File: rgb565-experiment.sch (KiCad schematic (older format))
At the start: 34 parts, among them J1 ST_SHIFTER_SOCKET, J2 Conn_01x02, SW1 SW_SPDT, U1 74HC00, U2 ST_SHIFTER, U3 ST_SHIFTER, U4 74HC245, U5 74LS257, U6 74HC245

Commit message: almost done routing
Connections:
- net at U1.3: now also U1.13; no longer U1.12
- net at U1.6: now also U1.12; no longer U1.13
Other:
- moved on the sheet: U1A, U1B
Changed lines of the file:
@@
 L 74xx:74HC00 U1
 U 1 1 61BD41CE
+P 9600 2150
+F 0 "U1" H 9600 2200 50  0000 C CNN
+F 1 "74HC00" H 9600 2100 50  0000 C CNN
+F 2 "Package_DIP:DIP-14_W7.62mm_Socket" H 9600 2150 50  0001 C CNN
+F 3 "http://www.ti.com/lit/gpn/sn74hc00" H 9600 2150 50  0001 C CNN
+	1    9600 2150
+	1    0    0    -1
+$EndComp
+$Comp
+L 74xx:74HC00 U1
+U 2 1 61BDB6F9
 P 9600 1700
 F 0 "U1" H 9600 1750 50  0000 C CNN
@@
 F 2 "Package_DIP:DIP-14_W7.62mm_Socket" H 9600 1700 50  0001 C CNN
 F 3 "http://www.ti.com/lit/gpn/sn74hc00" H 9600 1700 50  0001 C CNN
-	1    9600 1700
-	1    0    0    -1
-$EndComp
-$Comp
-L 74xx:74HC00 U1
-U 2 1 61BDB6F9
-P 9600 2150
-F 0 "U1" H 9600 2200 50  0000 C CNN
-F 1 "74HC00" H 9600 2100 50  0000 C CNN
-F 2 "Package_DIP:DIP-14_W7.62mm_Socket" H 9600 2150 50  0001 C CNN
-F 3 "http://www.ti.com/lit/gpn/sn74hc00" H 9600 2150 50  0001 C CNN
-	2    9600 2150
+	2    9600 1700
 	1    0    0    -1
 $EndComp
@@
 	1    0    0    -1
 $EndComp
+Text Label 9000 2050 0    50   ~ 0
+cs
+Wire Wire Line
+	9000 2050 9150 2050
 Text Label 9000 1600 0    50   ~ 0
-cs
-Wire Wire Line
-	9000 1600 9150 1600
-Text Label 9000 2050 0    50   ~ 0
 rxw
 Wire Wire Line
-	9300 2050 9150 2050
+	9300 1600 9150 1600
 Wire Wire Line
 	10900 1800 11500 1800
@@
 	11000 9500 11300 9500
 Wire Wire Line
+	9300 2250 9150 2250
+Wire Wire Line
+	9150 2250 9150 2050
+Connection ~ 9150 2050
+Wire Wire Line
+	9150 2050 9300 2050
+Wire Wire Line
 	9300 1800 9150 1800
 Wire Wire Line
@@
 Connection ~ 9150 1600
 Wire Wire Line
-	9150 1600 9300 1600
-Wire Wire Line
-	9300 2250 9150 2250
-Wire Wire Line
-	9150 2250 9150 2050
-Connection ~ 9150 2050
-Wire Wire Line
-	9150 2050 9000 2050
+	9150 1600 9000 1600
 Wire Wire Line
 	9900 2150 10100 2150

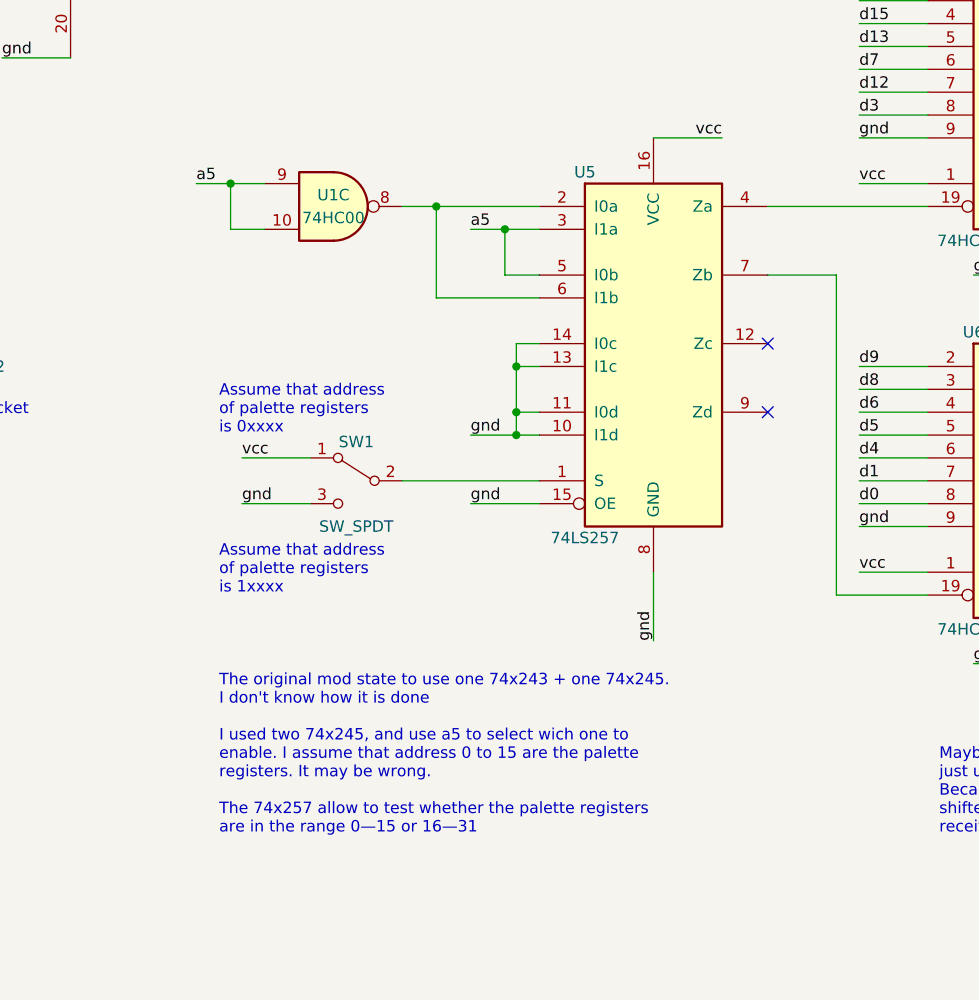
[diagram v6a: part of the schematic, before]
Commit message: Release Candidate 1 : modifications following experiments with the experimental version
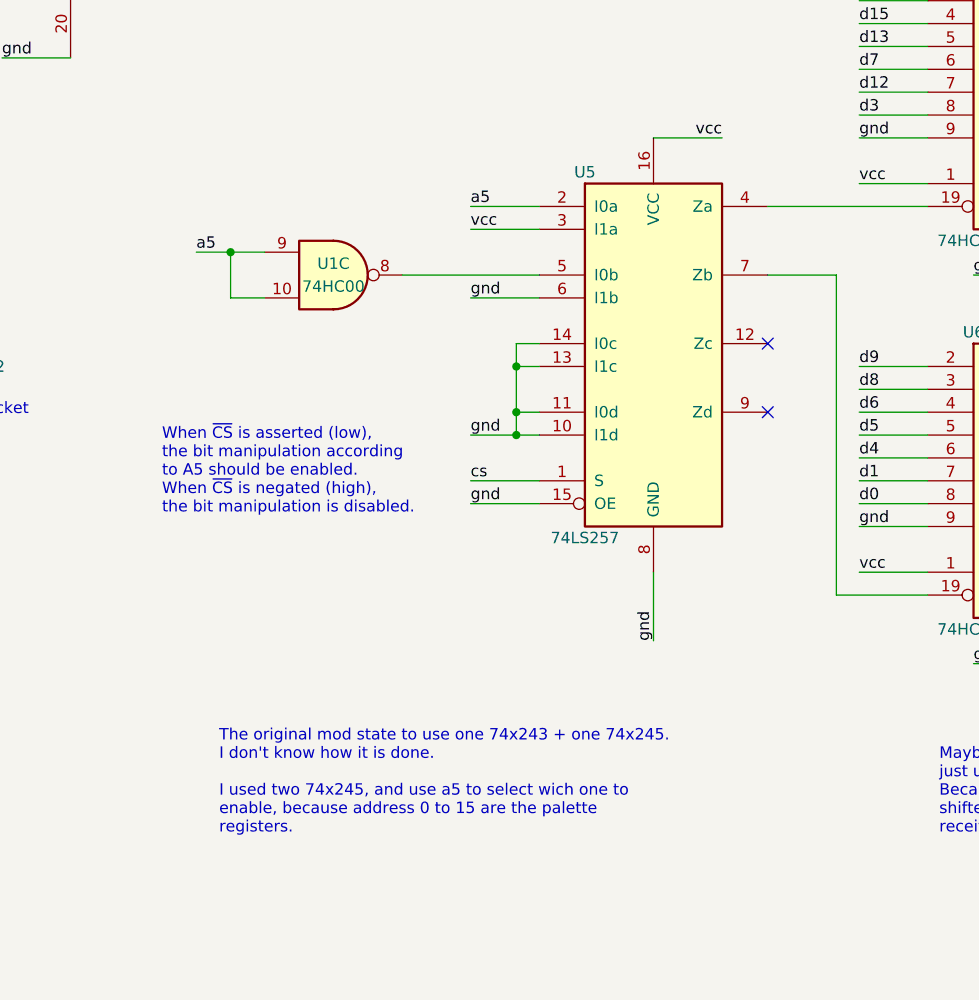
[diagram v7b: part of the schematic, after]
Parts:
- removed SW1: SW_SPDT, Connector_PinHeader_2.54mm:PinHeader_1x03_P2.54mm_Vertical, symbol Switch:SW_SPDT
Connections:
- net +5V: now also U5.3 (I1a)
- net GND: now also U5.6 (I1b)
- net a5: now also U5.2 (I0a); no longer U5.3 (I1a), U5.5 (I0b)
- net cs: now also U5.1 (S)
- new net: U1.8, U5.5 (I0b)
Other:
- note added: "The original mod state to use one 74x243 + one 74x245.\nI don't know how it is done.\n\nI used two 74x245, and use a5 to select wich one to \nenable, because address 0 to 15 are the palette\nregisters."
- note added: "When ~CS~ is asserted (low),\nthe bit manipulation according\nto A5 should be enabled.\nWhen ~CS~ is negated (high),\nthe bit manipulation is disabled."
- note removed: "Assume that address\nof palette registers \nis 0xxxx"
- note removed: "Assume that address\nof palette registers \nis 1xxxx"
- note removed: "The original mod state to use one 74x243 + one 74x245.\nI don't know how it is done\n\nI used two 74x245, and use a5 to select wich one to \nenable. I assume that address 0 to 15 are the palette\nregisters. It may be wrong.\n\nThe 74x257 allow to test whether the palette registers\nare in the range 0—15 or 16—31"
- moved on the sheet: U1C
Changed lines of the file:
@@
 Sheet 1 1
 Title "Experimental RGB-565 mod for the Atari ST"
-Date "2021-12-16"
-Rev "v1.0.0-xprc1"
+Date "2022-04-30"
+Rev "v1.0.0-rc1"
 Comp "Sporniket-Studio.com"
 Comment1 ""
@@
 L 74xx:74HC00 U1
 U 3 1 61BDF303
-P 3150 7000
-F 0 "U1" H 3150 7050 50  0000 C CNN
-F 1 "74HC00" H 3150 6950 50  0000 C CNN
-F 2 "Package_DIP:DIP-14_W7.62mm_Socket" H 3150 7000 50  0001 C CNN
-F 3 "http://www.ti.com/lit/gpn/sn74hc00" H 3150 7000 50  0001 C CNN
-	3    3150 7000
+P 3150 7300
+F 0 "U1" H 3150 7350 50  0000 C CNN
+F 1 "74HC00" H 3150 7250 50  0000 C CNN
+F 2 "Package_DIP:DIP-14_W7.62mm_Socket" H 3150 7300 50  0001 C CNN
+F 3 "http://www.ti.com/lit/gpn/sn74hc00" H 3150 7300 50  0001 C CNN
+	3    3150 7300
 	1    0    0    -1
 $EndComp
@@
 Wire Wire Line
 	10900 1800 11500 1800
-Text Label 2550 6900 0    50   ~ 0
+Text Label 2550 7200 0    50   ~ 0
 a5
 Wire Wire Line
-	2850 6900 2700 6900
+	2850 7200 2700 7200
 Text Notes 8600 1450 0    50   ~ 0
 ~CS2~ = ~CS~ OR R/~W~\nThe second shifter is prevented to drive the bus \nduring Read cycles
-Text Label 3750 7100 0    50   ~ 0
+Text Label 3750 7000 0    50   ~ 0
 a5
-Wire Wire Line
-	4050 7100 3900 7100
 $Comp
 L 74xx:74HC245 U4
@@
 	6250 7400 6550 7400
 Text Notes 2650 9750 0    50   ~ 0
-The original mod state to use one 74x243 + one 74x245.\nI don't know how it is done\n\nI used two 74x245, and use a5 to select wich one to \nenable. I assume that address 0 to 15 are the palette\nregisters. It may be wrong.\n\nThe 74x257 allow to test whether the palette registers\nare in the range 0—15 or 16—31
+The original mod state to use one 74x243 + one 74x245.\nI don't know how it is done.\n\nI used two 74x245, and use a5 to select wich one to \nenable, because address 0 to 15 are the palette\nregisters.
 Wire Wire Line
 	10300 1900 10100 1900
@@
 	4550 6700 4850 6700
 Wire Wire Line
-	2700 6900 2700 7100
-Wire Wire Line
-	2700 7100 2850 7100
-Connection ~ 2700 6900
-Wire Wire Line
-	2700 6900 2550 6900
-Wire Wire Line
-	3900 7100 3900 7300
-Wire Wire Line
-	3900 7300 4050 7300
-Connection ~ 3900 7100
-Wire Wire Line
-	3900 7100 3750 7100
-Wire Wire Line
-	4050 7000 3600 7000
-Wire Wire Line
-	3600 7000 3600 7400
-Wire Wire Line
-	3600 7400 4050 7400
-Connection ~ 3600 7000
-Wire Wire Line
-	3600 7000 3450 7000
+	2700 7200 2700 7400
+Wire Wire Line
+	2700 7400 2850 7400
+Connection ~ 2700 7200
+Wire Wire Line
+	2700 7200 2550 7200
 Text Label 3750 8000 0    50   ~ 0
 gnd
@@
 Wire Wire Line
 	3750 8300 4050 8300
-$Comp
-L Switch:SW_SPDT SW1
-U 1 1 61C533B5
-P 3250 8200
-F 0 "SW1" H 3250 8370 50  0000 C CNN
-F 1 "SW_SPDT" H 3250 8000 50  0000 C CNN
-F 2 "Connector_PinHeader_2.54mm:PinHeader_1x03_P2.54mm_Vertical" H 3250 8200 50  0001 C CNN
-F 3 "~" H 3250 8200 50  0001 C CNN
-	1    3250 8200
-	-1   0    0    -1
-$EndComp
 Wire Wire Line
 	5050 7300 5350 7300
-Text Label 2750 8300 0    50   ~ 0
-gnd
-Wire Wire Line
-	2750 8300 3050 8300
-Text Label 2750 8100 0    50   ~ 0
-vcc
-Wire Wire Line
-	3050 8100 2750 8100
-Wire Wire Line
-	3450 8200 4050 8200
-Text Notes 2650 8000 0    50   ~ 0
-Assume that address\nof palette registers  \nis 0xxxx
-Text Notes 2650 8700 0    50   ~ 0
-Assume that address\nof palette registers  \nis 1xxxx
+Text Label 3750 7400 0    50   ~ 0
+gnd
+Wire Wire Line
+	3750 7400 4050 7400
+Text Label 3750 7100 0    50   ~ 0
+vcc
+Wire Wire Line
+	4050 7100 3750 7100
+Text Notes 2400 8350 0    50   ~ 0
+When ~CS~ is asserted (low),\nthe bit manipulation according\nto A5 should be enabled.\nWhen ~CS~ is negated (high),\nthe bit manipulation is disabled.
 NoConn ~ 5050 7600
 NoConn ~ 5050 7900
@@
 Wire Notes Line
 	7450 5450 7450 5850
+Text Label 3750 8200 0    50   ~ 0
+cs
+Wire Wire Line
+	3750 8200 4050 8200
+Wire Wire Line
+	3450 7300 4050 7300
+Wire Wire Line
+	3750 7000 4050 7000
 $EndSCHEMATC
